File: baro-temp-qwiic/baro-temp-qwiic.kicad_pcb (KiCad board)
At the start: 2 copper layers, 10 x 18.4 mm, 8 parts, among them J1 Conn_01x04_Male, U1 BMP388, U2 TMP102xxDRL

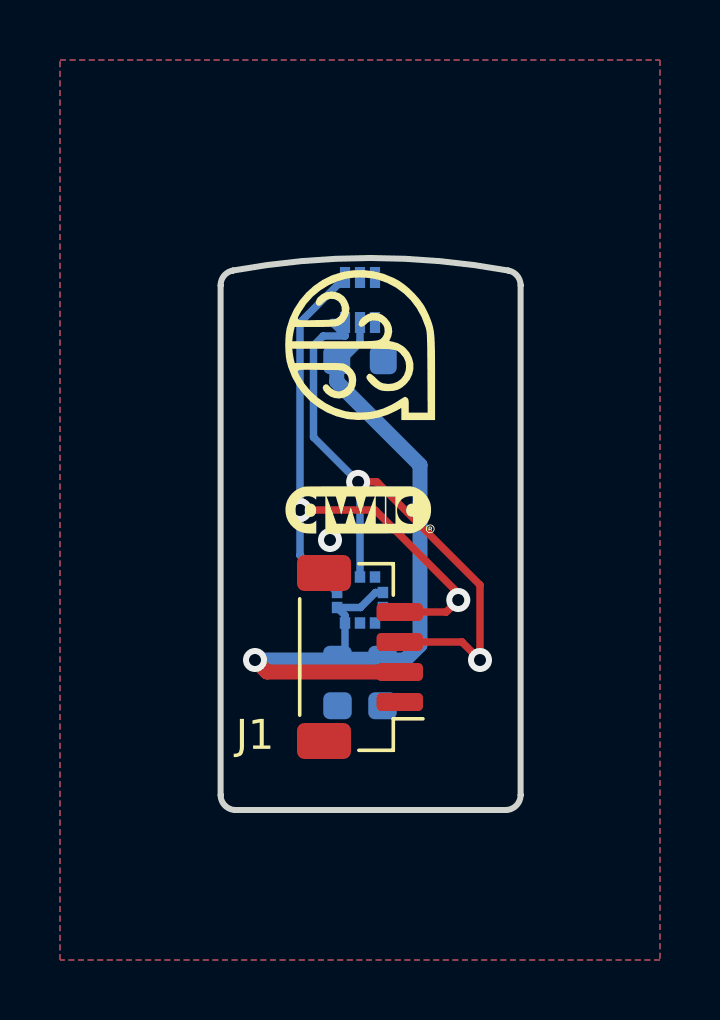
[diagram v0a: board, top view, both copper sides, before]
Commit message: Made board smaller to fit better into probe.
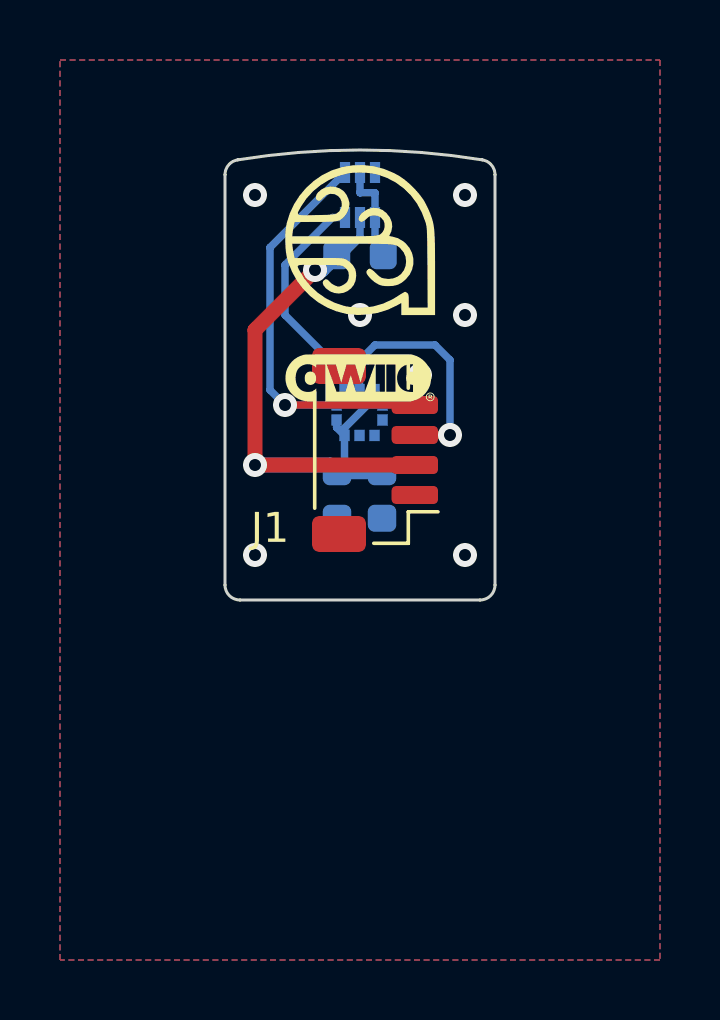
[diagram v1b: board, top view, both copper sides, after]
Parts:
- moved J1 6.92 mm to (0.50, -12.0)
- moved C1 6.25 mm to (0.73, -10.5)
- moved C2 6.25 mm to (-0.77, -10.5)
- moved U1 6.25 mm to (-0.02, -13.2)
- moved G*** 4.40 mm to (0.00, -14.4)
- moved C3 3.50 mm to (0.00, -18.5)
- moved G*** 3.50 mm to (0.00, -19.0)
- moved U2 3.50 mm to (0.00, -20.5)
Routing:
- net /SDA: track 21.5 -> 15.5 mm, vias 2 -> 1
- net /SCL: track 20.4 -> 15.0 mm, vias 2 -> 1
- net +3V3: track 27.0 -> 23.4 mm, vias 1 -> 2
- net GND: track 0.00 -> 3.36 mm, vias 1 -> 7
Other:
- board size 10 x 18.4 mm -> 9 x 15 mm
- board text added: "Airball Temp/Baro 2023-03-04"
- board text added: "Copyright (C) 2023, The Airball Authors"
- board text removed: "Airball Temp/Baro Copyright (C) 2023, The Airball Authors 2023-03-03"

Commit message: Minor appearance finishing touches.
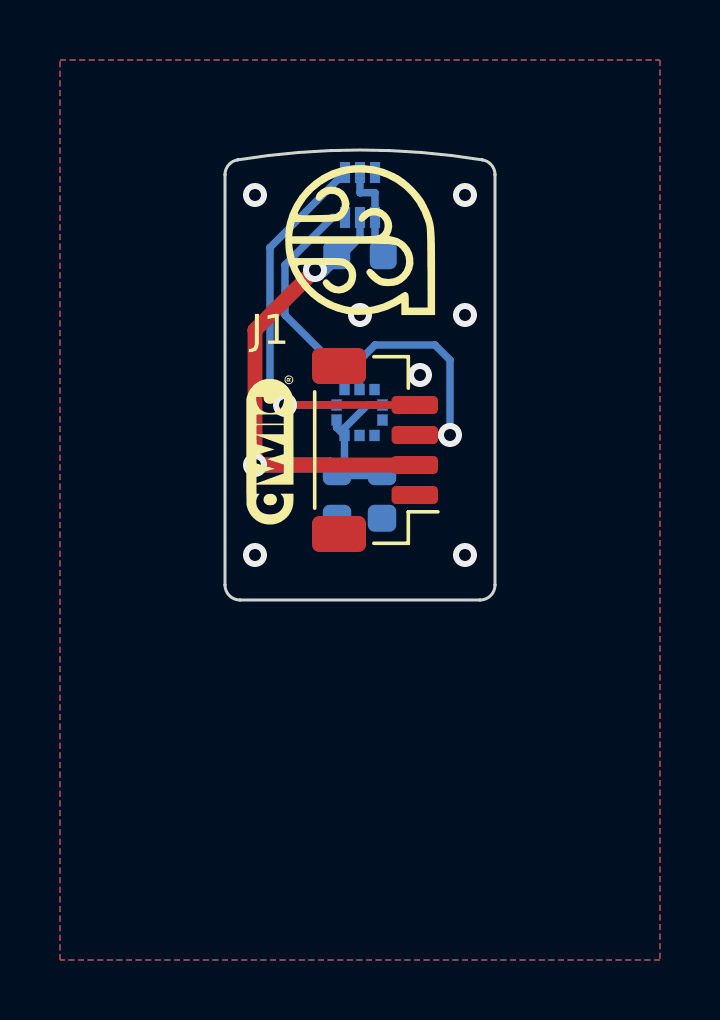
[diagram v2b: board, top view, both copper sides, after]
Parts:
- moved G*** 3.84 mm to (-3.00, -12.0), turned to 90 degrees
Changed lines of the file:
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@@
   (net 6 "unconnected-(U2-Pad3)")
   (footprint "airball-hardware:qwiic-logo-5mm" (layer "F.Cu")
-    (at 0 -14.4)
+    (at -3 -12 90)
     (attr board_only exclude_from_pos_files exclude_from_bom)
-    (fp_text reference "G***" (at 0 0) (layer "F.SilkS") hide
+    (fp_text reference "G***" (at 0 0 90) (layer "F.SilkS") hide
       (effects (font (size 1.524 1.524) (thickness 0.3)))
     )
-    (fp_text value "LOGO" (at 0.75 0) (layer "F.SilkS") hide
+    (fp_text value "LOGO" (at 0.75 0 90) (layer "F.SilkS") hide
       (effects (font (size 1.524 1.524) (thickness 0.3)))
     )
@@
     (property "Sheetname" "")
     (attr smd)
-    (fp_text reference "J1" (at -2.6 -3.5 180) (layer "F.SilkS")
+    (fp_text reference "J1" (at 4 -3.5 180) (layer "F.SilkS")
       (effects (font (size 1 1) (thickness 0.15)))
     )

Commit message: Finished design and made fab outputs.
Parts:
- moved C3 0.25 mm to (0.00, -18.2)
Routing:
- net /SDA: track 15.5 -> 14.7 mm
- net /SCL: track 15.0 -> 15.8 mm
- net GND: vias 7 -> 10
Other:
- board text added: "Airball Temp/Baro 2023-03-14"
- board text added: "Copyright © 2023, The Airball authors"
- board text removed: "Airball Temp/Baro 2023-03-04"
- board text removed: "Copyright (C) 2023, The Airball Authors"
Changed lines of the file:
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@@
       (outputformat 1)
       (mirror false)
-      (drillshape 1)
+      (drillshape 0)
       (scaleselection 1)
       (outputdirectory "")
@@
     (pad "4" smd roundrect (at 1.5 1.325 90) (size 0.6 1.55) (layers "F.Cu" "F.Paste" "F.Mask") (roundrect_rratio 0.25)
       (net 4 "/SCL") (pinfunction "Pin_4") (pintype "passive"))
-    (pad "MP" smd roundrect (at 2.8 -1.2 90) (size 1.2 1.8) (layers "F.Cu" "F.Paste" "F.Mask") (roundrect_rratio 0.208333))
-    (pad "MP" smd roundrect (at -2.8 -1.2 90) (size 1.2 1.8) (layers "F.Cu" "F.Paste" "F.Mask") (roundrect_rratio 0.208333))
+    (pad "MP" smd roundrect (at 2.8 -1.2 90) (size 1.2 1.8) (layers "F.Cu" "F.Paste" "F.Mask") (roundrect_rratio 0.2083333333))
+    (pad "MP" smd roundrect (at -2.8 -1.2 90) (size 1.2 1.8) (layers "F.Cu" "F.Paste" "F.Mask") (roundrect_rratio 0.2083333333))
     (model "/home/ihab/airball-hardware/lib/airball-hardware.pretty/BM04B-SRSS.step"
       (offset (xyz 0 1.25 0))
@@
   )
   (footprint "Capacitor_SMD:C_0603_1608Metric" (layer "B.Cu")
-    (at 0 -18.5)
+    (at 0 -18.25)
     (descr "Capacitor SMD 0603 (1608 Metric), square (rectangular) end terminal, IPC_7351 nominal, (Body size source: IPC-SM-782 page 76, https://www.pcb-3d.com/wordpress/wp-content/uploads/ipc-sm-782a_amendment_1_and_2.pdf), generated with kicad-footprint-generator")
     (tags "capacitor")
@@
   (gr_line (start 4.5 -7.5) (end 4.5 -21.176615) (layer "Edge.Cuts") (width 0.1))
   (gr_arc (start 4.080321 -21.670121) (mid 4.380896 -21.500528) (end 4.5 -21.176615) (layer "Edge.Cuts") (width 0.1))
-  (gr_text "Airball Temp/Baro\n2023-03-04" (at -3 -14.5 90) (layer "B.SilkS")
+  (gr_text "Airball Temp/Baro\n2023-03-14" (at -3 -14.5 90) (layer "B.SilkS")
     (effects (font (size 0.5 0.5) (thickness 0.0625)) (justify mirror))
   )
-  (gr_text "Copyright (C) 2023,\nThe Airball Authors" (at 3 -15 90) (layer "B.SilkS")
+  (gr_text "Copyright © 2023,\nThe Airball authors" (at 3 -15 90) (layer "B.SilkS")
     (effects (font (size 0.5 0.5) (thickness 0.0625)) (justify mirror))
   )
-  (segment (start -3.5 -11.5) (end -3.5 -16) (width 0.5) (layer "F.Cu") (net 1))
-  (segment (start -3.5 -16) (end -1.5 -18) (width 0.5) (layer "F.Cu") (net 1))
+  (segment (start -1.663248 -17.586752) (end -3.5 -15.75) (width 0.5) (layer "F.Cu") (net 1))
+  (segment (start -1.5755 -17.586752) (end -1.663248 -17.586752) (width 0.5) (layer "F.Cu") (net 1))
+  (segment (start -3.5 -15.75) (end -3.5 -11.5) (width 0.5) (layer "F.Cu") (net 1))
   (segment (start 1.825 -11.5) (end -3.5 -11.5) (width 0.5) (layer "F.Cu") (net 1))
   (via (at -3.5 -11.5) (size 0.8) (drill 0.4) (layers "F.Cu" "B.Cu") (net 1))
-  (via (at -1.5 -18) (size 0.8) (drill 0.4) (layers "F.Cu" "B.Cu") (net 1))
+  (via (at -1.5755 -17.586752) (size 0.8) (drill 0.4) (layers "F.Cu" "B.Cu") (net 1))
+  (segment (start -1.5755 -17.586752) (end -0.912252 -18.25) (width 0.5) (layer "B.Cu") (net 1))
   (segment (start -0.780192 -13) (end -0.780192 -12.75) (width 0.25) (layer "B.Cu") (net 1))
   (segment (start -0.765192 -11.275) (end 0.734808 -11.275) (width 0.5) (layer "B.Cu") (net 1))
   (segment (start 0 -19.75) (end 0 -19.08) (width 0.25) (layer "B.Cu") (net 1))
-  (segment (start -1.5 -18) (end -1.275 -18) (width 0.5) (layer "B.Cu") (net 1))
   (segment (start -0.780192 -12.75) (end -0.515192 -12.485) (width 0.25) (layer "B.Cu") (net 1))
   (segment (start 0.25 -13.5) (end 0.749808 -13.5) (width 0.25) (layer "B.Cu") (net 1))
-  (segment (start -1.275 -18) (end -0.775 -18.5) (width 0.5) (layer "B.Cu") (net 1))
-  (segment (start -0.58 -18.5) (end -0.775 -18.5) (width 0.25) (layer "B.Cu") (net 1))
   (segment (start 0 -19.08) (end -0.58 -18.5) (width 0.25) (layer "B.Cu") (net 1))
   (segment (start -0.990192 -11.5) (end -0.765192 -11.275) (width 0.5) (layer "B.Cu") (net 1))
   (segment (start -0.515192 -11.525) (end -0.765192 -11.275) (width 0.25) (layer "B.Cu") (net 1))
+  (segment (start -0.912252 -18.25) (end -0.775 -18.25) (width 0.5) (layer "B.Cu") (net 1))
   (segment (start -0.515192 -12.485) (end -0.515192 -11.525) (width 0.25) (layer "B.Cu") (net 1))
   (segment (start -0.515192 -12.485) (end -0.515192 -12.734808) (width 0.25) (layer "B.Cu") (net 1))
@@
   (segment (start -0.515192 -12.734808) (end 0.25 -13.5) (width 0.25) (layer "B.Cu") (net 1))
   (via (at -3.5 -20.5) (size 0.8) (drill 0.4) (layers "F.Cu" "B.Cu") (free) (net 2))
+  (via (at -2.25 -15) (size 0.8) (drill 0.4) (layers "F.Cu" "B.Cu") (free) (net 2))
   (via (at -3.5 -8.5) (size 0.8) (drill 0.4) (layers "F.Cu" "B.Cu") (free) (net 2))
   (via (at 3.5 -16.5) (size 0.8) (drill 0.4) (layers "F.Cu" "B.Cu") (free) (net 2))
+  (via (at -2.5 -12.5) (size 0.8) (drill 0.4) (layers "F.Cu" "B.Cu") (free) (net 2))
   (via (at 3.5 -8.5) (size 0.8) (drill 0.4) (layers "F.Cu" "B.Cu") (free) (net 2))
   (via (at 2 -14.5) (size 0.8) (drill 0.4) (layers "F.Cu" "B.Cu") (free) (net 2))
   (via (at 3.5 -20.5) (size 0.8) (drill 0.4) (layers "F.Cu" "B.Cu") (free) (net 2))
   (via (at 0 -16.5) (size 0.8) (drill 0.4) (layers "F.Cu" "B.Cu") (free) (net 2))
+  (via (at -2.2 -19.5) (size 0.8) (drill 0.4) (layers "F.Cu" "B.Cu") (free) (net 2))
   (segment (start 0 -21.25) (end 0 -20.58) (width 0.25) (layer "B.Cu") (net 2))
   (segment (start 0.5 -19.75) (end 0.5 -18.775) (width 0.25) (layer "B.Cu") (net 2))
@@
   (segment (start 1.825 -12.5) (end 3 -12.5) (width 0.25) (layer "F.Cu") (net 3))
   (via (at 3 -12.5) (size 0.8) (drill 0.4) (layers "F.Cu" "B.Cu") (net 3))
-  (segment (start -2.5 -18.17) (end -2.5 -16.5) (width 0.25) (layer "B.Cu") (net 3))
-  (segment (start -0.92 -19.75) (end -2.5 -18.17) (width 0.25) (layer "B.Cu") (net 3))
+  (segment (start -0.5 -19.75) (end -0.777817 -19.75) (width 0.25) (layer "B.Cu") (net 3))
   (segment (start -0.015192 -14.984808) (end -0.015192 -14.015) (width 0.25) (layer "B.Cu") (net 3))
-  (segment (start -0.984808 -14.984808) (end -0.015192 -14.984808) (width 0.25) (layer "B.Cu") (net 3))
-  (segment (start -0.5 -19.75) (end -0.92 -19.75) (width 0.25) (layer "B.Cu") (net 3))
+  (segment (start -1.800305 -18.727512) (end -1.800305 -18.725) (width 0.25) (layer "B.Cu") (net 3))
   (segment (start 3 -15) (end 2.5 -15.5) (width 0.25) (layer "B.Cu") (net 3))
   (segment (start 0.5 -15.5) (end -0.015192 -14.984808) (width 0.25) (layer "B.Cu") (net 3))
+  (segment (start -1.800305 -18.725) (end -2.25 -18.275305) (width 0.25) (layer "B.Cu") (net 3))
+  (segment (start -2.25 -18.275305) (end -2.25 -17.219616) (width 0.25) (layer "B.Cu") (net 3))
   (segment (start 3 -12.5) (end 3 -15) (width 0.25) (layer "B.Cu") (net 3))
-  (segment (start -2.5 -16.5) (end -0.984808 -14.984808) (width 0.25) (layer "B.Cu") (net 3))
+  (segment (start -0.777817 -19.75) (end -1.800305 -18.727512) (width 0.25) (layer "B.Cu") (net 3))
   (segment (start 2.5 -15.5) (end 0.5 -15.5) (width 0.25) (layer "B.Cu") (net 3))
+  (segment (start -2.25 -17.219616) (end -0.015192 -14.984808) (width 0.25) (layer "B.Cu") (net 3))
   (segment (start 1.825 -13.5) (end -2.5 -13.5) (width 0.25) (layer "F.Cu") (net 4))
   (via (at -2.5 -13.5) (size 0.8) (drill 0.4) (layers "F.Cu" "B.Cu") (net 4))
+  (segment (start -3.25 -14.25) (end -2.5 -13.5) (width 0.25) (layer "B.Cu") (net 4))
   (segment (start -0.780192 -13.5) (end -2.5 -13.5) (width 0.25) (layer "B.Cu") (net 4))
-  (segment (start -3 -18.75) (end -3 -14) (width 0.25) (layer "B.Cu") (net 4))
-  (segment (start -3 -14) (end -2.5 -13.5) (width 0.25) (layer "B.Cu") (net 4))
-  (segment (start -0.5 -21.25) (end -3 -18.75) (width 0.25) (layer "B.Cu") (net 4))
+  (segment (start -1.5 -21.25) (end -3.25 -19.5) (width 0.25) (layer "B.Cu") (net 4))
+  (segment (start -0.5 -21.25) (end -1.5 -21.25) (width 0.25) (layer "B.Cu") (net 4))
+  (segment (start -3.25 -19.5) (end -3.25 -14.25) (width 0.25) (layer "B.Cu") (net 4))
   (zone (net 2) (net_name "GND") (layers F&B.Cu) (hatch edge 0.508)
     (connect_pads (clearance 0.15))
     (min_thickness 0.15) (filled_areas_thickness no)
-    (fill yes (thermal_gap 0.5) (thermal_bridge_width 0.5))
+    (fill yes (thermal_gap 0.15) (thermal_bridge_width 0.5))
     (polygon
       (pts

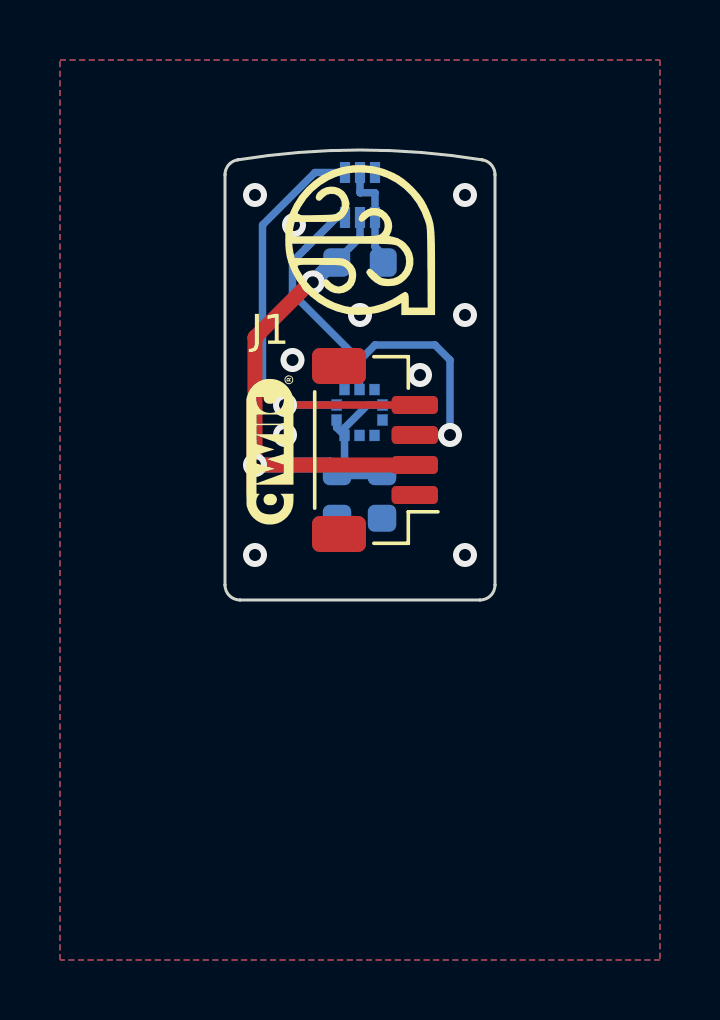
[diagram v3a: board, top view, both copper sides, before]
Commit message: Re-spun board for better solder mask clearance.
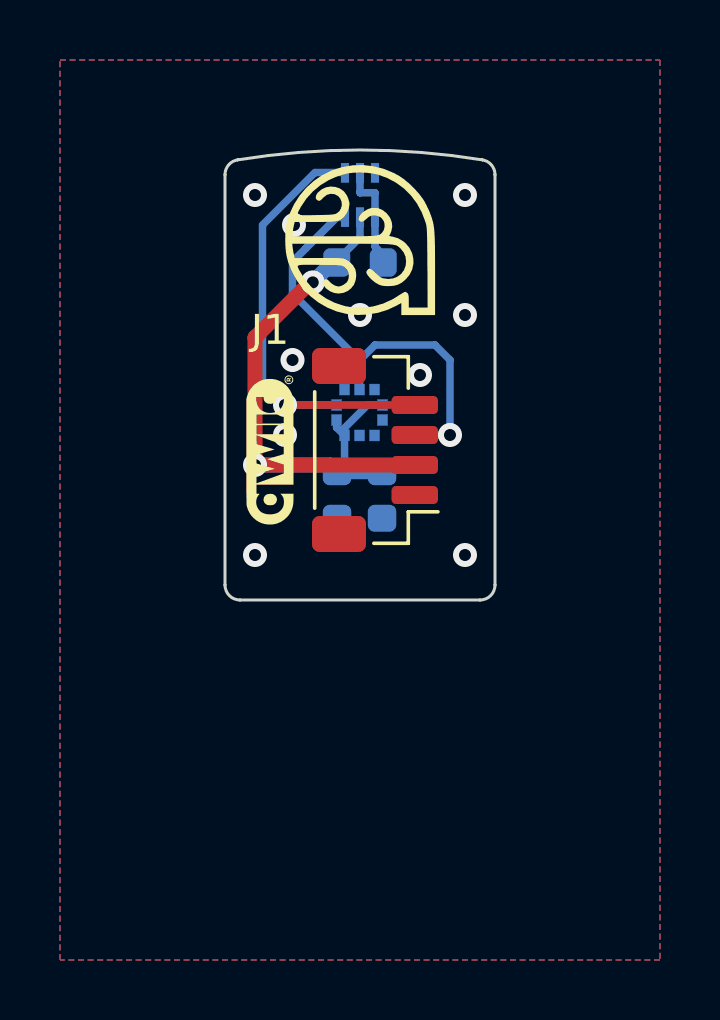
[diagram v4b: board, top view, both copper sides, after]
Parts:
- U1: value BMP388 -> PQFN50P200X200X80-10N
- U2: footprint Package_TO_SOT_SMD:SOT-563 -> airball-hardware:TMP102 - SOT50P160X60-6N
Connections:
- U2 pad 1: /SCL -> /SDA
- U2 pad 6: /SDA -> /SCL
